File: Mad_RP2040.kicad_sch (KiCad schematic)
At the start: 22 parts, among them J1 USB_C_Receptacle, SW1 SW_SPST, SW2 SW_SPST, U0 PCB, U1 ECMF02-2AMX6

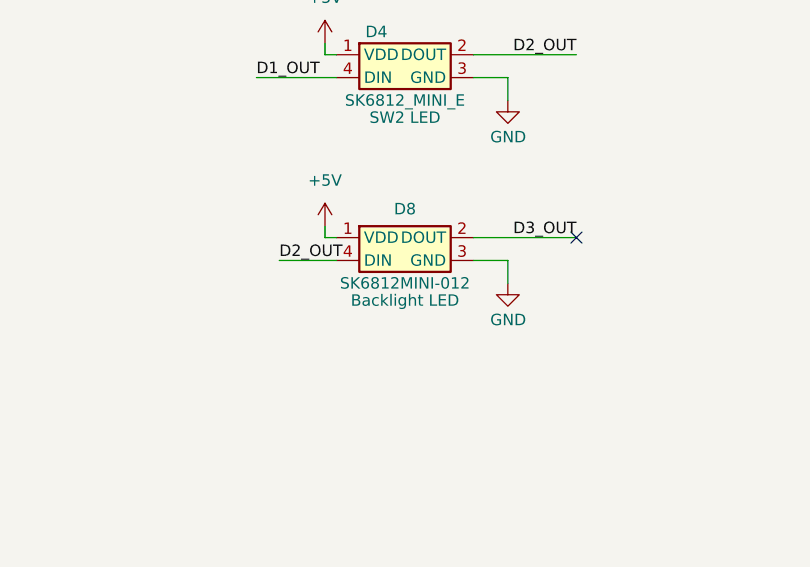
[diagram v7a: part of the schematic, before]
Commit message: BOM update, add lcsc pn to  componenets.
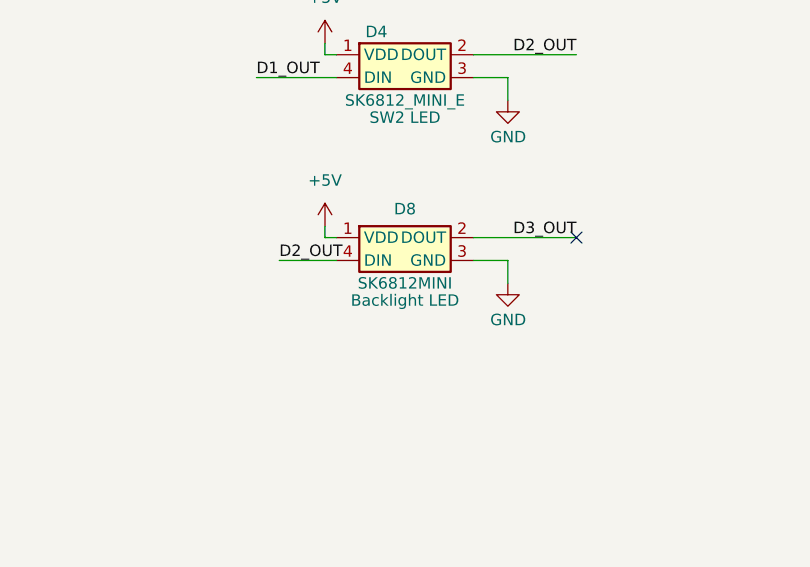
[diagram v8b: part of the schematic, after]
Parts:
- D1, D2: LCSC PN (none) -> C435829
- D3, D4: LCSC PN (none) -> C5149201
- D8: value SK6812MINI-012 -> SK6812MINI; LCSC PN (none) -> C2886570; MPN SK6812MINI-012 -> SK6812MINI
- FB1, FB2: LCSC PN (none) -> C160974
- FID1, FID2, FID3, H1, H2, U0: now left out of the parts list
- J1: LCSC PN (none) -> C3020560
- R1, R2: LCSC PN (none) -> C105872
- SW1, SW2: LCSC PN (none) -> C2803348; MPN 4958 -> CPG151101S11
- U1: LCSC PN (none) -> C2651144
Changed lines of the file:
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@@
 			)
 		)
+		(property "LCSC PN" "C5149201"
+			(at 228.6 88.9 0)
+			(effects
+				(font
+					(size 1.27 1.27)
+				)
+				(hide yes)
+			)
+		)
 		(pin "1"
 		)
@@
 		(unit 1)
 		(exclude_from_sim no)
-		(in_bom yes)
+		(in_bom no)
 		(on_board yes)
 		(dnp no)
@@
 			)
 		)
-		(property "Value" "SK6812MINI-012"
+		(property "Value" "SK6812MINI"
 			(at 228.6 132.08 0)
 			(effects
@@
 			)
 		)
-		(property "MPN" "SK6812MINI-012"
+		(property "MPN" "SK6812MINI"
+			(at 228.6 128.27 0)
+			(effects
+				(font
+					(size 1.27 1.27)
+				)
+				(hide yes)
+			)
+		)
+		(property "LCSC PN" "C2886570"
 			(at 228.6 128.27 0)
 			(effects
@@
 			)
 		)
-		(property "MPN" "4958"
+		(property "MPN" "CPG151101S11"
 			(at 232.41 62.23 0)
 			(effects
@@
 			)
 		)
+		(property "LCSC PN" "C2803348"
+			(at 232.41 62.23 0)
+			(effects
+				(font
+					(size 1.27 1.27)
+				)
+				(hide yes)
+			)
+		)
 		(pin "1"
 		)
@@
 		(unit 1)
 		(exclude_from_sim no)
-		(in_bom yes)
+		(in_bom no)
 		(on_board yes)
 		(dnp no)
@@
 			)
 		)
+		(property "LCSC PN" "C3020560"
+			(at 33.02 68.58 0)
+			(effects
+				(font
+					(size 1.27 1.27)
+				)
+				(hide yes)
+			)
+		)
 		(pin "A1"
 		)
@@
 			)
 		)
+		(property "LCSC PN" "C5149201"
+			(at 228.6 107.95 0)
+			(effects
+				(font
+					(size 1.27 1.27)
+				)
+				(hide yes)
+			)
+		)
 		(pin "1"
 		)
@@
 			)
 		)
+		(property "LCSC PN" "C435829"
+			(at 223.52 62.23 0)
+			(effects
+				(font
+					(size 1.27 1.27)
+				)
+				(hide yes)
+			)
+		)
 		(pin "1"
 		)
@@
 			)
 		)
-		(property "MPN" "4958"
+		(property "MPN" "CPG151101S11"
 			(at 233.68 74.93 0)
 			(effects
@@
 			)
 		)
+		(property "LCSC PN" "C2803348"
+			(at 233.68 74.93 0)
+			(effects
+				(font
+					(size 1.27 1.27)
+				)
+				(hide yes)
+			)
+		)
 		(pin "1"
 		)
@@
 			)
 		)
+		(property "LCSC PN" "C160974"
+			(at 80.01 93.98 0)
+			(effects
+				(font
+					(size 1.27 1.27)
+				)
+				(hide yes)
+			)
+		)
 		(pin "2"
 		)
@@
 			)
 		)
+		(property "LCSC PN" "C435829"
+			(at 224.79 74.93 0)
+			(effects
+				(font
+					(size 1.27 1.27)
+				)
+				(hide yes)
+			)
+		)
 		(pin "1"
 		)
@@
 		(unit 1)
 		(exclude_from_sim no)
-		(in_bom yes)
+		(in_bom no)
 		(on_board yes)
 		(dnp no)
@@
 		(unit 1)
 		(exclude_from_sim no)
-		(in_bom yes)
+		(in_bom no)
 		(on_board yes)
 		(dnp no)
@@
 		(unit 1)
 		(exclude_from_sim no)
-		(in_bom yes)
+		(in_bom no)
 		(on_board yes)
 		(dnp no)
@@
 			)
 		)
+		(property "LCSC PN" "C105872"
+			(at 52.07 60.96 0)
+			(effects
+				(font
+					(size 1.27 1.27)
+				)
+				(hide yes)
+			)
+		)
 		(pin "1"
 		)
@@
 		(unit 1)
 		(exclude_from_sim no)
-		(in_bom yes)
+		(in_bom no)
 		(on_board yes)
 		(dnp no)
@@
 			)
 		)
+		(property "LCSC PN" "C2651144"
+			(at 80.01 71.12 0)
+			(effects
+				(font
+					(size 1.27 1.27)
+				)
+				(hide yes)
+			)
+		)
 		(pin "3"
 		)
@@
 			)
 		)
+		(property "LCSC PN" "C160974"
+			(at 80.01 34.29 0)
+			(effects
+				(font
+					(size 1.27 1.27)
+				)
+				(hide yes)
+			)
+		)
 		(pin "2"
 		)
@@
 			(at 52.07 58.42 0)
 			(effects
+				(font
+					(size 1.27 1.27)
+				)
+				(hide yes)
+			)
+		)
+		(property "LCSC PN" "C105872"
+			(at 52.07 58.42 0)
+			(effects
